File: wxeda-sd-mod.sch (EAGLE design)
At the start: 11 parts, among them U1 SD_CARD

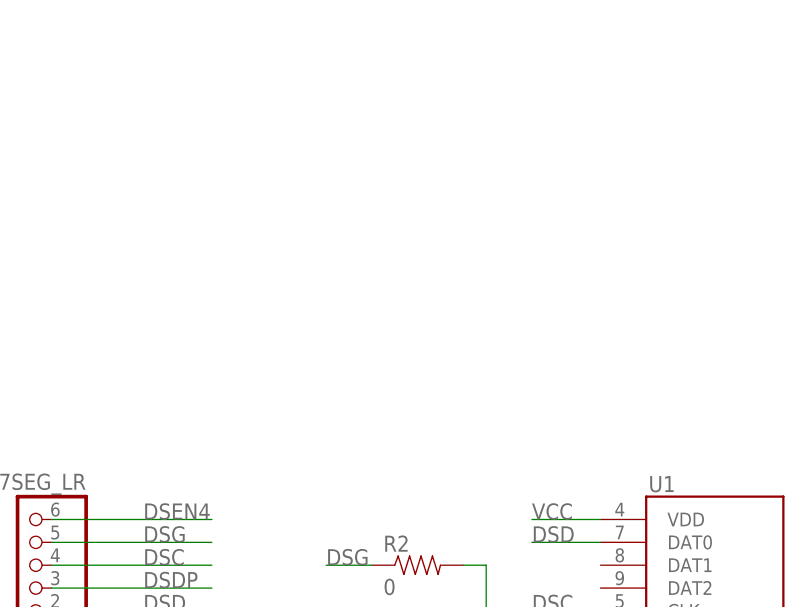
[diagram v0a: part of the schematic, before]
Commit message: Added pull-up resistors
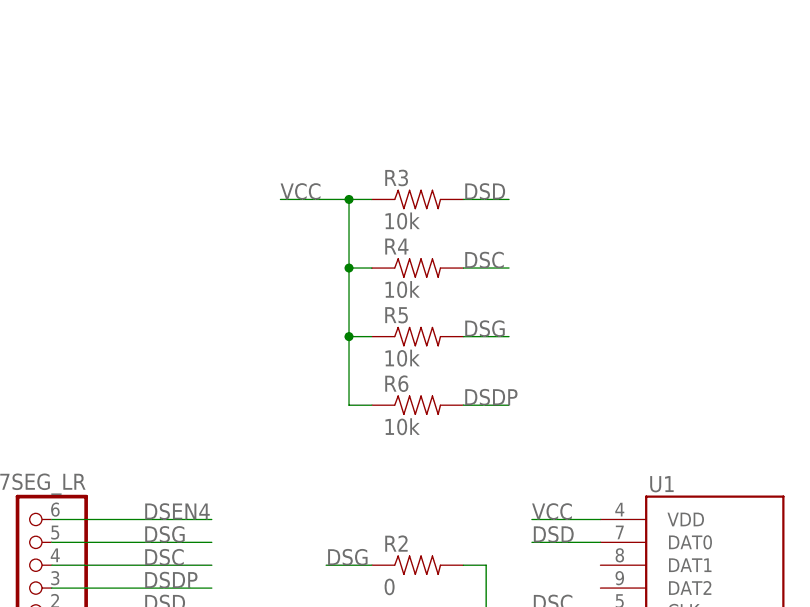
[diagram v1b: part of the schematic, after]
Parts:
- added R3, R4, R5, R6: 10k, SparkFun-Passives:RESISTORAXIAL-0.3
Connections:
- net DSC: now also R4.2
- net DSD: now also R3.2
- net DSDP: now also R6.2
- net DSG: now also R5.2
- net VCC: now also R3.1, R4.1, R5.1, R6.1

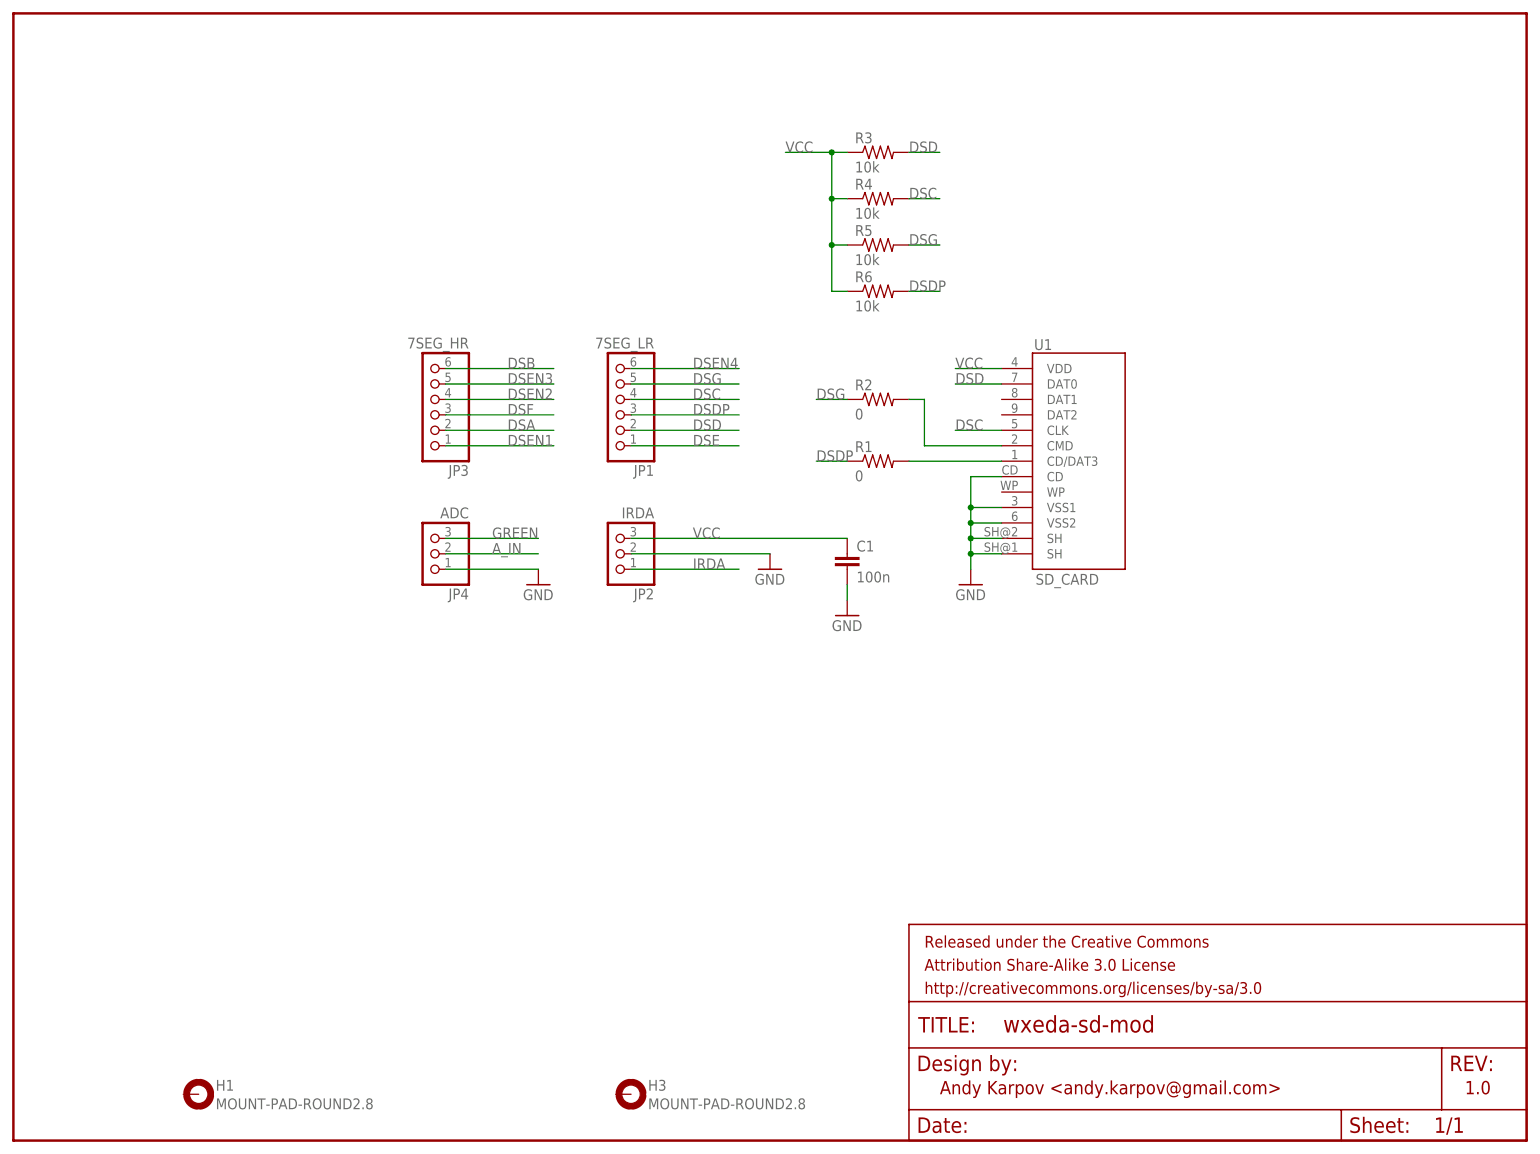
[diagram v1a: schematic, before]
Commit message: Added tape in/out and tv out
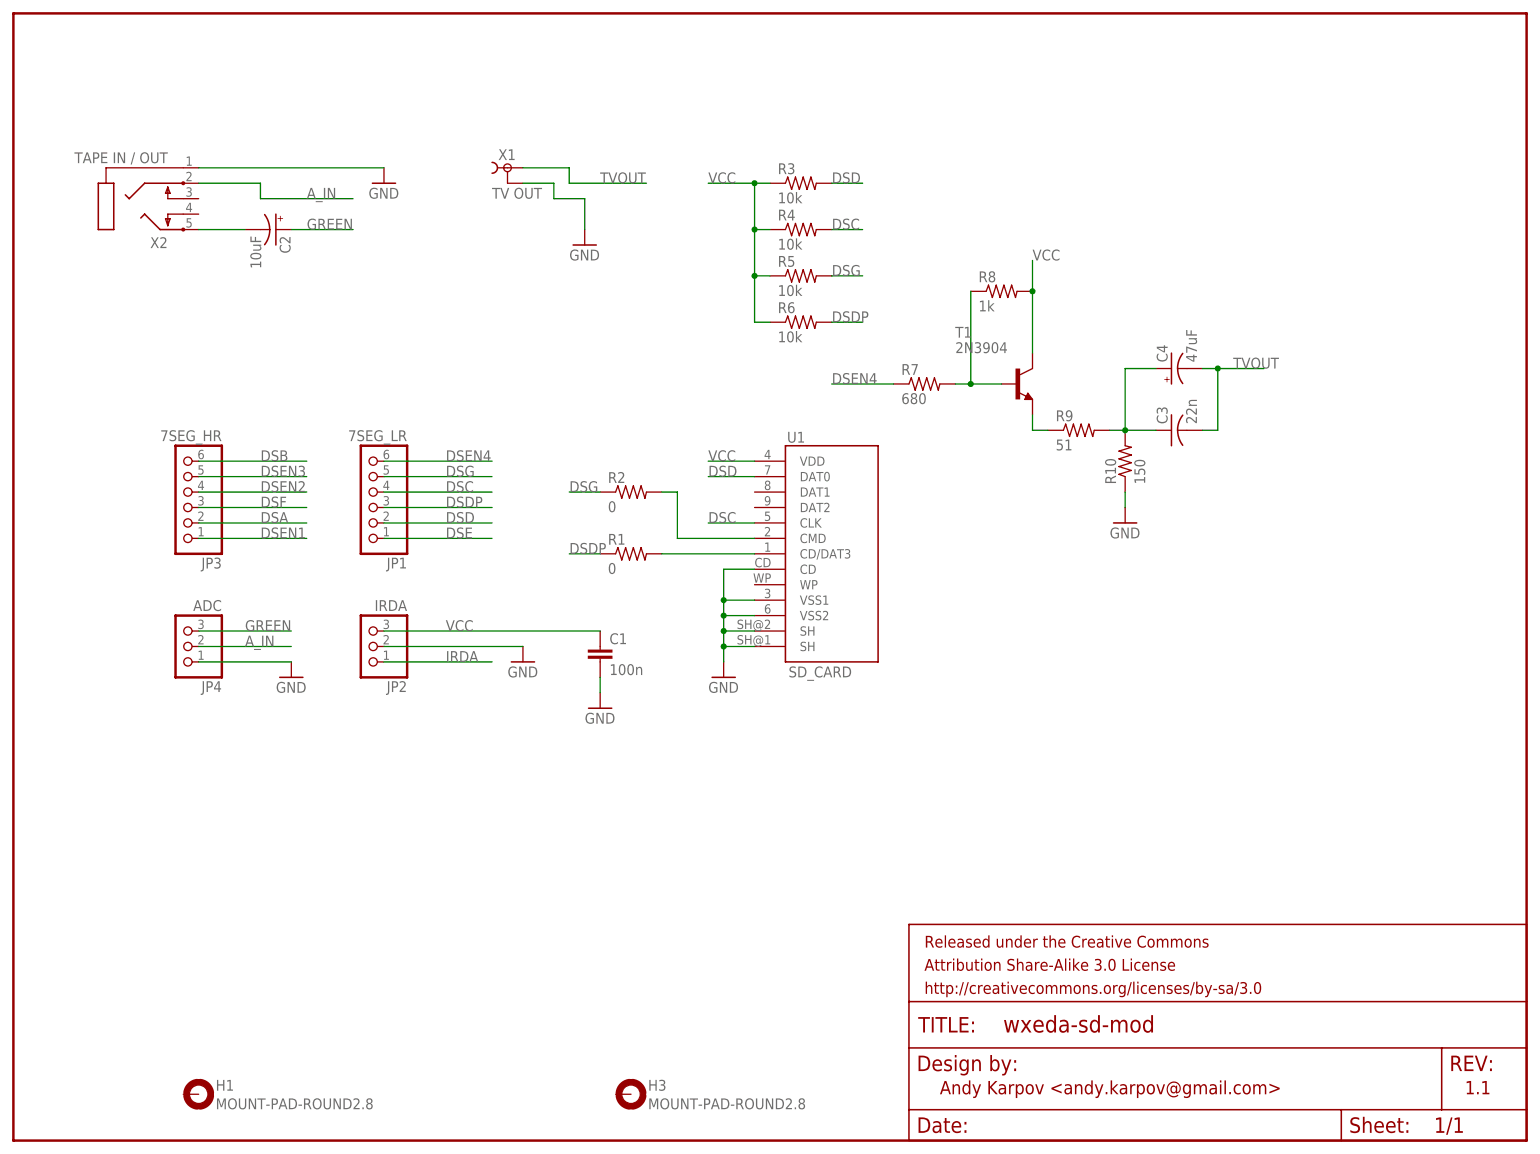
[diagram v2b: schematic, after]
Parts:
- added C2: 10uF, adafruit:CPOL-USE5-8.5
- added C3: 22n, adafruit:C-US050-025X075
- added C4: 47uF, adafruit:CPOL-USE5-8.5
- added R10: 150, adafruit:R-US_0204/7
- added R7: 680, adafruit:R-US_0204/7
- added R8: 1k, adafruit:R-US_0204/7
- added R9: 51, adafruit:R-US_0204/7
- added T1: 2N3904, transistor:2N3904
- added X1: TV OUT, con-hirschmann:TOBU3
- added X2: TAPE IN / OUT, adafruit:STEREOJACK
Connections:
- new net N$2: R7.2, R8.1, T1.B
- new net N$4: C2.-, X2.5
- new net N$7: R9.1, T1.E
- new net N$8: C3.1, C4.+, R10.2, R9.2
- new net TVOUT: C3.2, C4.-, X1.1
- net A_IN: now also X2.2
- net DSEN4: now also R7.1
- net GND: now also R10.1, X1.2, X2.1
- net GREEN: now also C2.+
- net VCC: now also R8.2, T1.C
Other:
- note added: "1.1"
- note removed: "1.0"
- moved on the sheet: C1, JP1, JP2, JP3, JP4, R1, R2, R3, R4, R5, R6, U1

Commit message: small improvements
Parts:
- added C5: 10uF, adafruit:CPOL-USE5-8.5
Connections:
- new net N$6: C5.-, X2.2
- net A_IN: now also C5.+; no longer X2.2
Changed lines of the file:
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@@
 <part name="X1" library="con-hirschmann" deviceset="TOBU3" device="" value="TV OUT"/>
 <part name="X2" library="adafruit" deviceset="STEREOJACK" device="" value="TAPE IN / OUT"/>
+<part name="C5" library="adafruit" deviceset="CPOL-US" device="E5-8.5" value="10uF"/>
 </parts>
 <sheets>
@@
 <instance part="R5" gate="G$1" x="129.54" y="142.24"/>
 <instance part="R6" gate="G$1" x="129.54" y="134.62"/>
-<instance part="GND5" gate="1" x="60.96" y="157.48"/>
+<instance part="GND5" gate="1" x="60.96" y="162.56"/>
 <instance part="C2" gate="G$1" x="43.18" y="149.86" rot="R270"/>
 <instance part="GND7" gate="1" x="93.98" y="147.32"/>
@@
 <instance part="X1" gate="B" x="81.28" y="160.02"/>
 <instance part="X2" gate="1" x="17.78" y="152.4" rot="R180"/>
+<instance part="C5" gate="G$1" x="43.18" y="160.02" rot="R270"/>
 </instances>
 <busses>
@@
 <pinref part="X2" gate="1" pin="1"/>
 <pinref part="GND5" gate="1" pin="GND"/>
-<wire x1="30.48" y1="160.02" x2="60.96" y2="160.02" width="0.1524" layer="91"/>
+<wire x1="30.48" y1="160.02" x2="30.48" y2="165.1" width="0.1524" layer="91"/>
+<wire x1="30.48" y1="165.1" x2="60.96" y2="165.1" width="0.1524" layer="91"/>
 </segment>
 </net>
@@
 </segment>
 <segment>
-<wire x1="40.64" y1="154.94" x2="55.88" y2="154.94" width="0.1524" layer="91"/>
-<label x="48.26" y="154.94" size="1.778" layer="95"/>
-<pinref part="X2" gate="1" pin="2"/>
-<wire x1="30.48" y1="157.48" x2="40.64" y2="157.48" width="0.1524" layer="91"/>
-<wire x1="40.64" y1="157.48" x2="40.64" y2="154.94" width="0.1524" layer="91"/>
+<wire x1="45.72" y1="160.02" x2="55.88" y2="160.02" width="0.1524" layer="91"/>
+<label x="48.26" y="160.02" size="1.778" layer="95"/>
+<pinref part="C5" gate="G$1" pin="+"/>
 </segment>
 </net>
@@
 </segment>
 </net>
+<net name="N$6" class="0">
+<segment>
+<pinref part="X2" gate="1" pin="2"/>
+<pinref part="C5" gate="G$1" pin="-"/>
+<wire x1="30.48" y1="157.48" x2="38.1" y2="157.48" width="0.1524" layer="91"/>
+<wire x1="38.1" y1="157.48" x2="38.1" y2="160.02" width="0.1524" layer="91"/>
+</segment>
+</net>

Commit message: minor changes
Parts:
- H1, H3: value MOUNT-PAD-ROUND2.8 -> SEW_HOLE; device holes:MOUNT-PAD-ROUND2.8 -> LilyPad-Wearables:SEW_HOLE
- R10, R7, R8, R9: device adafruit:R-US_0204/7 -> SparkFun-Passives:RESISTORAXIAL-0.3
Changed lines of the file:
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@@
 <part name="GND3" library="SparkFun-Aesthetics" deviceset="GND" device=""/>
 <part name="FRAME1" library="SparkFun-Aesthetics" deviceset="FRAME-LETTER" device=""/>
-<part name="H1" library="holes" deviceset="MOUNT-PAD-ROUND" device="2.8"/>
-<part name="H3" library="holes" deviceset="MOUNT-PAD-ROUND" device="2.8"/>
+<part name="H1" library="LilyPad-Wearables" deviceset="SEW_HOLE" device=""/>
+<part name="H3" library="LilyPad-Wearables" deviceset="SEW_HOLE" device=""/>
 <part name="R1" library="SparkFun-Passives" deviceset="RESISTOR" device="AXIAL-0.3" value="0"/>
 <part name="R2" library="SparkFun-Passives" deviceset="RESISTOR" device="AXIAL-0.3" value="0"/>
@@
 <part name="GND7" library="SparkFun-Aesthetics" deviceset="GND" device=""/>
 <part name="T1" library="transistor" deviceset="2N3904" device=""/>
-<part name="R7" library="adafruit" deviceset="R-US_" device="0204/7" value="680"/>
-<part name="R8" library="adafruit" deviceset="R-US_" device="0204/7" value="1k"/>
-<part name="R9" library="adafruit" deviceset="R-US_" device="0204/7" value="51"/>
-<part name="R10" library="adafruit" deviceset="R-US_" device="0204/7" value="150"/>
+<part name="R7" library="SparkFun-Passives" deviceset="RESISTOR" device="AXIAL-0.3" value="680"/>
+<part name="R8" library="SparkFun-Passives" deviceset="RESISTOR" device="AXIAL-0.3" value="1k"/>
+<part name="R9" library="SparkFun-Passives" deviceset="RESISTOR" device="AXIAL-0.3" value="51"/>
+<part name="R10" library="SparkFun-Passives" deviceset="RESISTOR" device="AXIAL-0.3" value="150"/>
 <part name="C3" library="adafruit" deviceset="C-US" device="050-025X075" value="22n"/>
 <part name="C4" library="adafruit" deviceset="CPOL-US" device="E5-8.5" value="47uF"/>

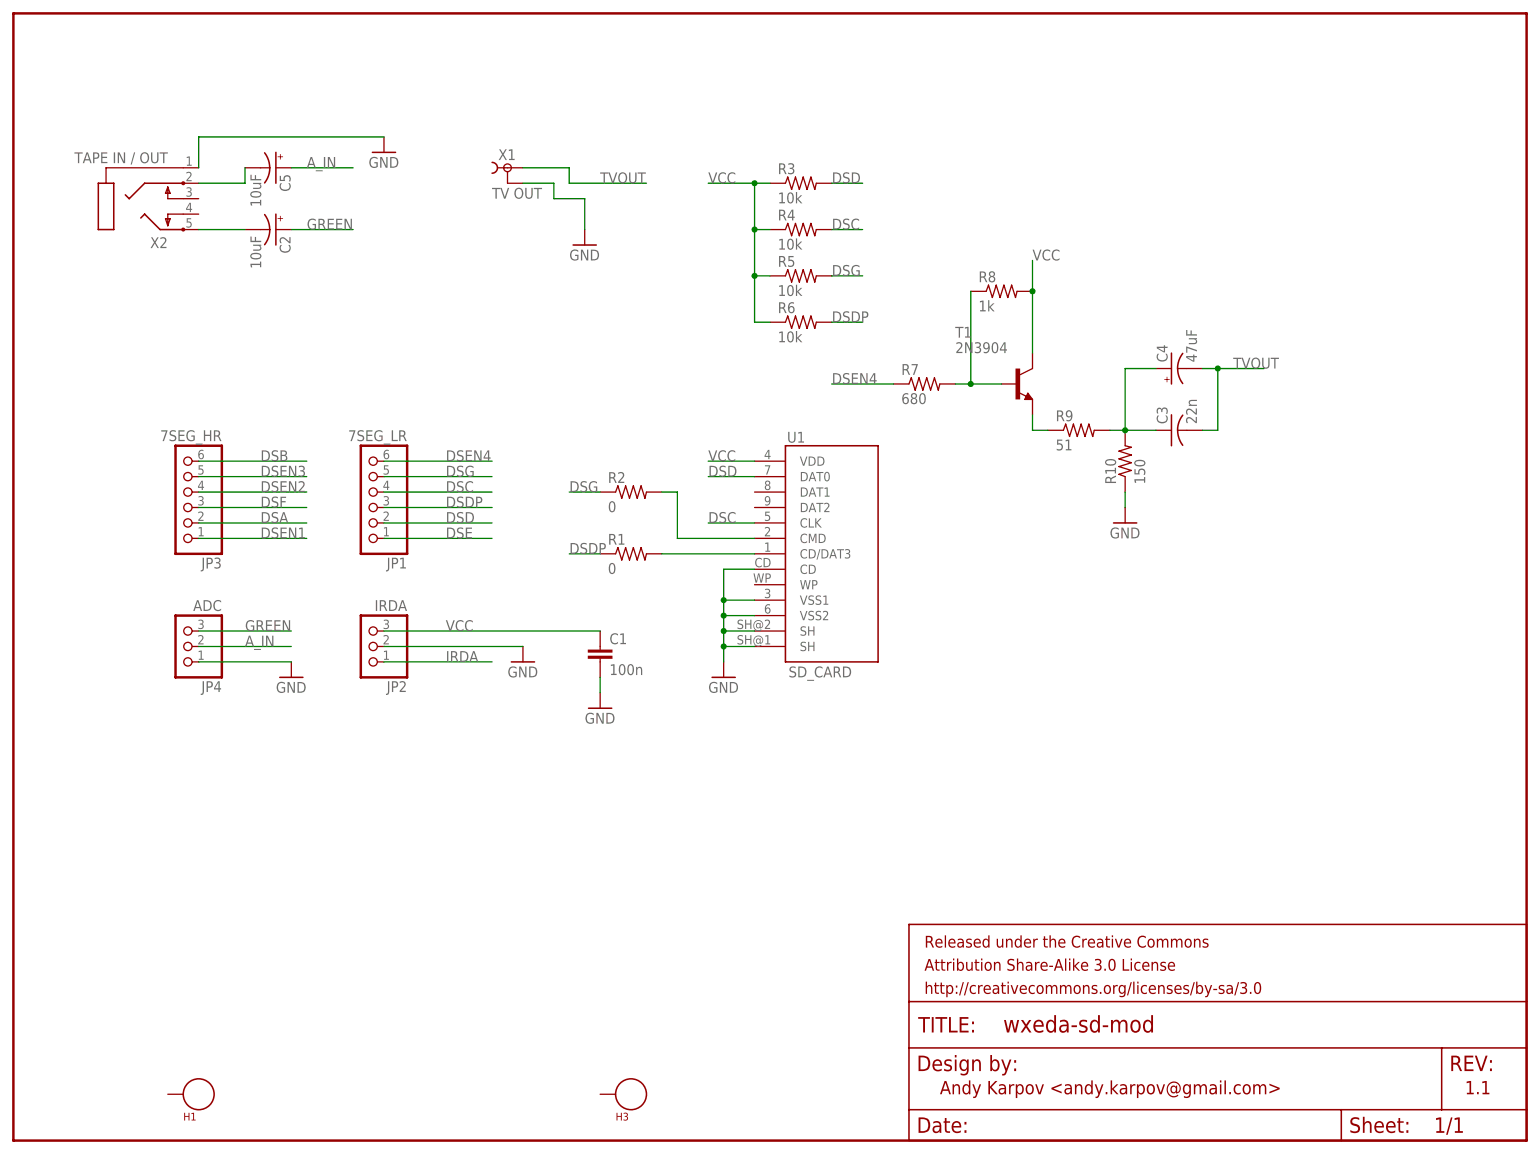
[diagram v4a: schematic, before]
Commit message: Added stereo out
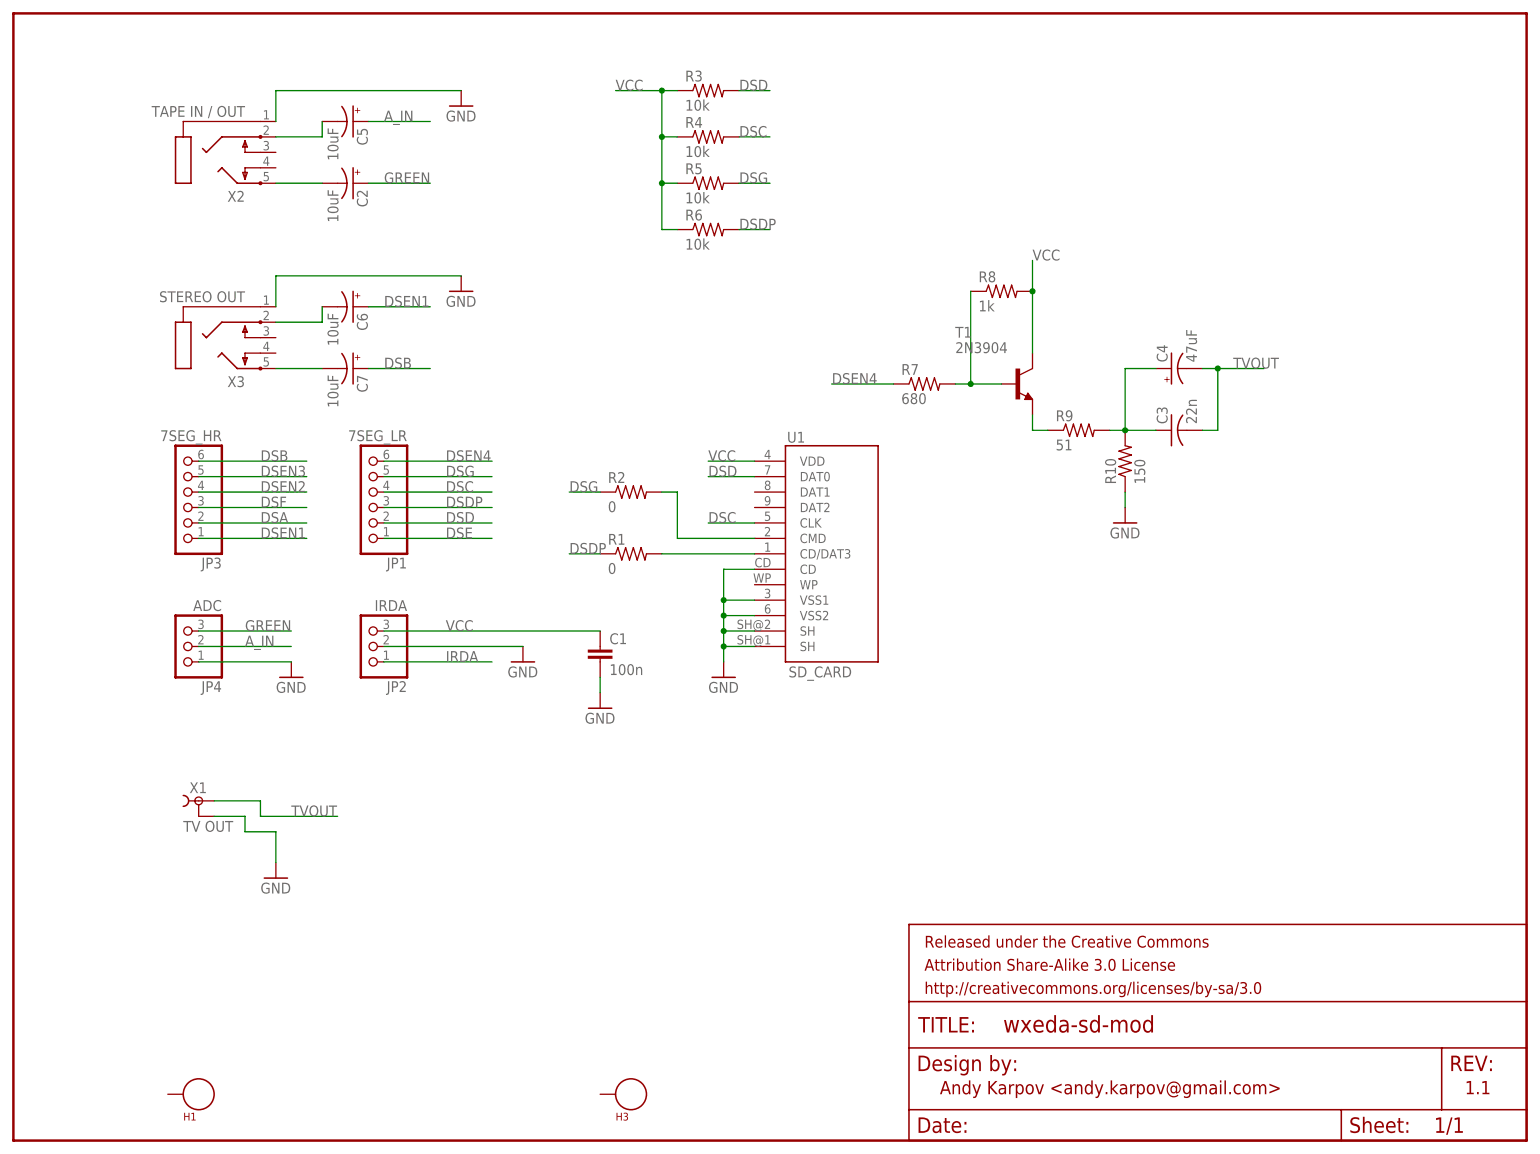
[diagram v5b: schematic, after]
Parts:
- added C6, C7: 10uF, adafruit:CPOL-USE2,5-6E
- added X3: STEREO OUT, adafruit:STEREOJACK
- C2, C4, C5: device adafruit:CPOL-USE5-8.5 -> adafruit:CPOL-USE2,5-6E
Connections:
- new net N$11: C7.-, X3.5
- new net N$9: C6.-, X3.2
- net DSB: now also C7.+
- net DSEN1: now also C6.+
- net GND: now also X3.1
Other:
- moved on the sheet: C2, C5, R3, R4, R5, R6, X1, X2

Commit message: small improvements
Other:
- note added: "1.0 RCA"
- note removed: "1.1"
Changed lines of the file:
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@@
 <plain>
 <text x="152.4" y="7.62" size="2.1844" layer="94">Andy Karpov &lt;andy.karpov@gmail.com&gt;</text>
-<text x="238.76" y="7.62" size="2.1844" layer="94">1.1</text>
+<text x="236.22" y="7.62" size="1.778" layer="94">1.0 RCA</text>
 </plain>
 <instances>
